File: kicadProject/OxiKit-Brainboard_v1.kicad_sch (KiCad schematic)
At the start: 60 parts, among them J1 OXY-Sensor, J10 Valve3, J11 Air Compresssor, J2 Jack-DC, J3 UART, J4 Fan1, J5 Fan2, J6 I2C, J7 Valve1, J8 Valve2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

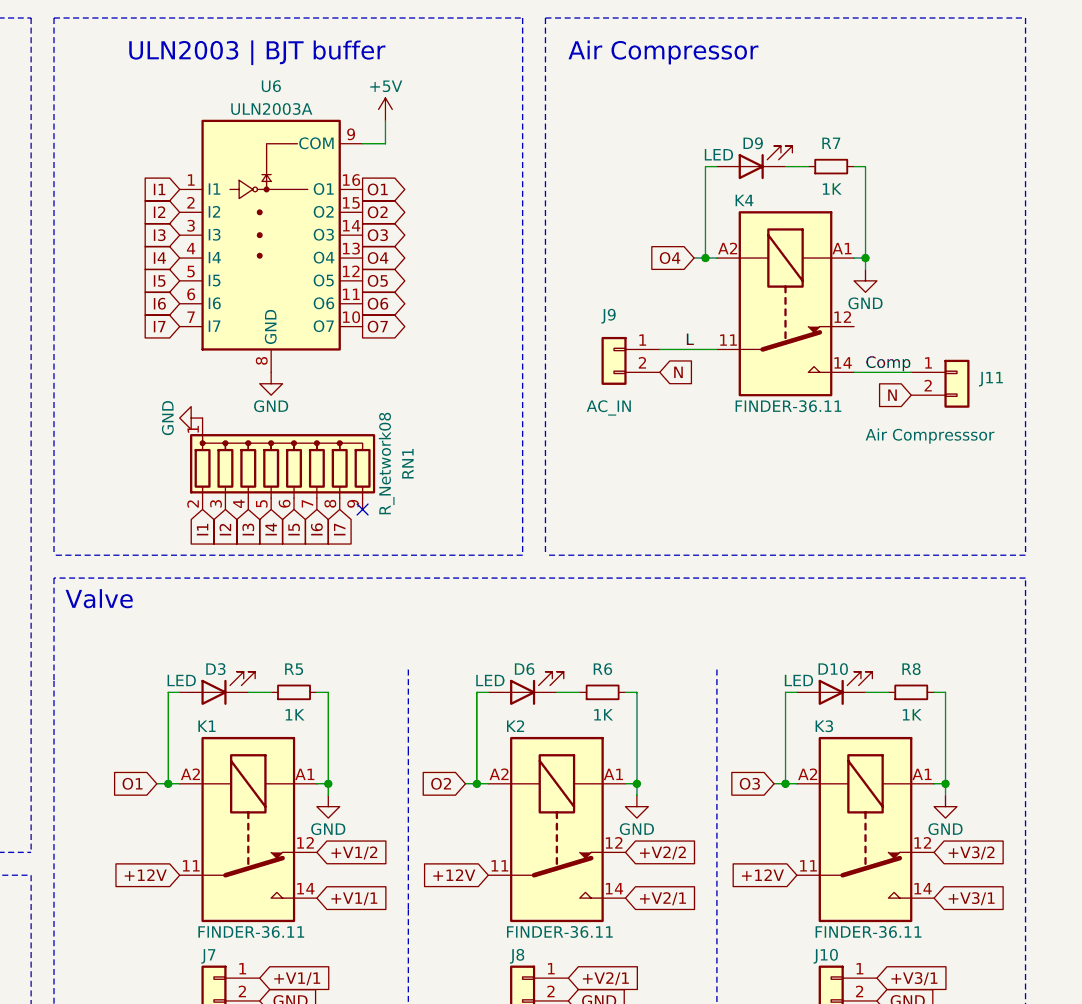
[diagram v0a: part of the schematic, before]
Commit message: #1 ULN2003 and Relay connection Fixed, Indication LED of Relay also updated
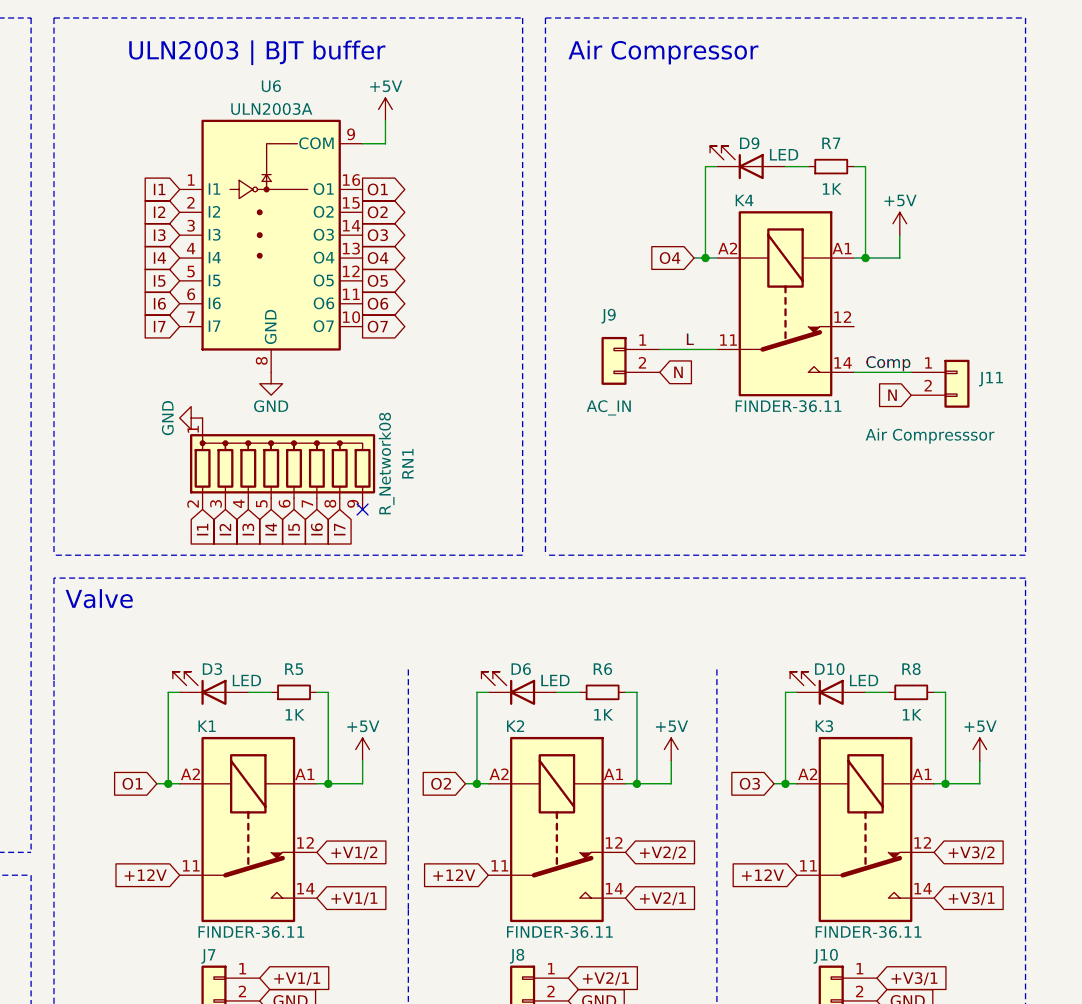
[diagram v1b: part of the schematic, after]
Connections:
- net +5V: now also K1.A1, K2.A1, K3.A1, K4.A1, R5.2, R6.2, R7.2, R8.2
- net GND: no longer K1.A1, K2.A1, K3.A1, K4.A1, R5.2, R6.2, R7.2, R8.2
- net O1: now also D3.1 (K); no longer D3.2 (A)
- net O2: now also D6.1 (K); no longer D6.2 (A)
- net O3: now also D10.1 (K); no longer D10.2 (A)
- net O4: now also D9.1 (K); no longer D9.2 (A)
- net at R7.1: now also D9.2 (A); no longer D9.1 (K)
- net at R5.1: now also D3.2 (A); no longer D3.1 (K)
- net at R8.1: now also D10.2 (A); no longer D10.1 (K)
- net at R6.1: now also D6.2 (A); no longer D6.1 (K)
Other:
- moved on the sheet: D10, D3, D6, D9

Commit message: OSHW Logo Added
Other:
- note added: "An Open Source Oxygen Concentrator Brain Board. https://github.com/shridattdudhat/Oxikit-Brainboard https://shridattdudhat.github.io"
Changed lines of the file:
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@@
     (effects (font (size 2 2)) (justify left bottom))
+  )
+  (text "An Open Source Oxygen Concentrator Brain Board.\n\nhttps://github.com/shridattdudhat/Oxikit-Brainboard\n\nhttps://shridattdudhat.github.io"
+    (at 177.8 177.8 0)
+    (effects (font (size 1.27 1.27)) (justify left bottom))
   )
   (text "ULN2003 | BJT buffer" (at 212.09 19.05 180)
@@
     (pin "1")
     (pin "2")
+  )
+  (symbol (lib_id "Graphic:Logo_Open_Hardware_Small") (at 267.97 173.99 0) (unit 1)
+    (in_bom yes) (on_board yes) (fields_autoplaced)
+    (property "Reference" "#LOGO?" (id 0) (at 267.97 167.005 0)
+      (effects (font (size 1.27 1.27)) hide)
+    )
+    (property "Value" "Logo_Open_Hardware_Small" (id 1) (at 267.97 179.705 0)
+      (effects (font (size 1.27 1.27)) hide)
+    )
+    (property "Footprint" "" (id 2) (at 267.97 173.99 0)
+      (effects (font (size 1.27 1.27)) hide)
+    )
+    (property "Datasheet" "~" (id 3) (at 267.97 173.99 0)
+      (effects (font (size 1.27 1.27)) hide)
+    )
   )
   (symbol (lib_id "Regulator_Linear:LM7805_TO220") (at 57.15 168.91 0) (unit 1)
@@
   )
   (symbol_instances
+    (path "/988d75da-a129-499a-90d8-6f1a62061a11"
+      (reference "#LOGO?") (unit 1) (value "Logo_Open_Hardware_Small") (footprint "")
+    )
     (path "/a3cbf87e-78b6-4799-99e8-c537c4416e24"
       (reference "#PWR01") (unit 1) (value "GND") (footprint "")

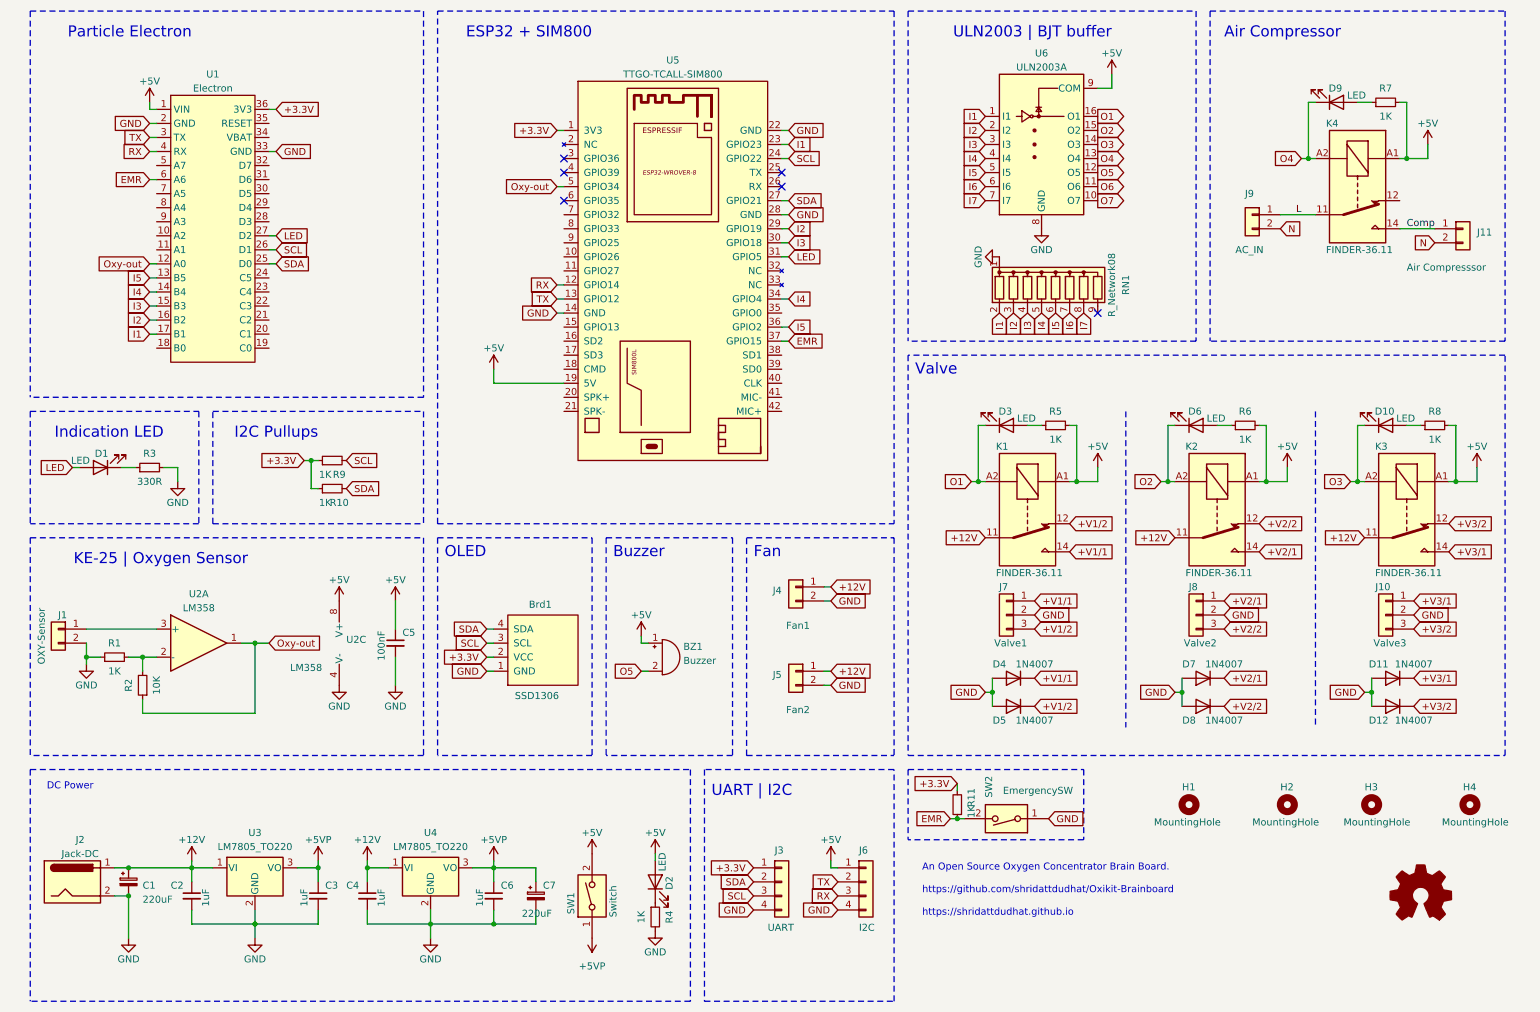
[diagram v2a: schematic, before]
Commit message: ABP Honeywell Pressure Sensor added
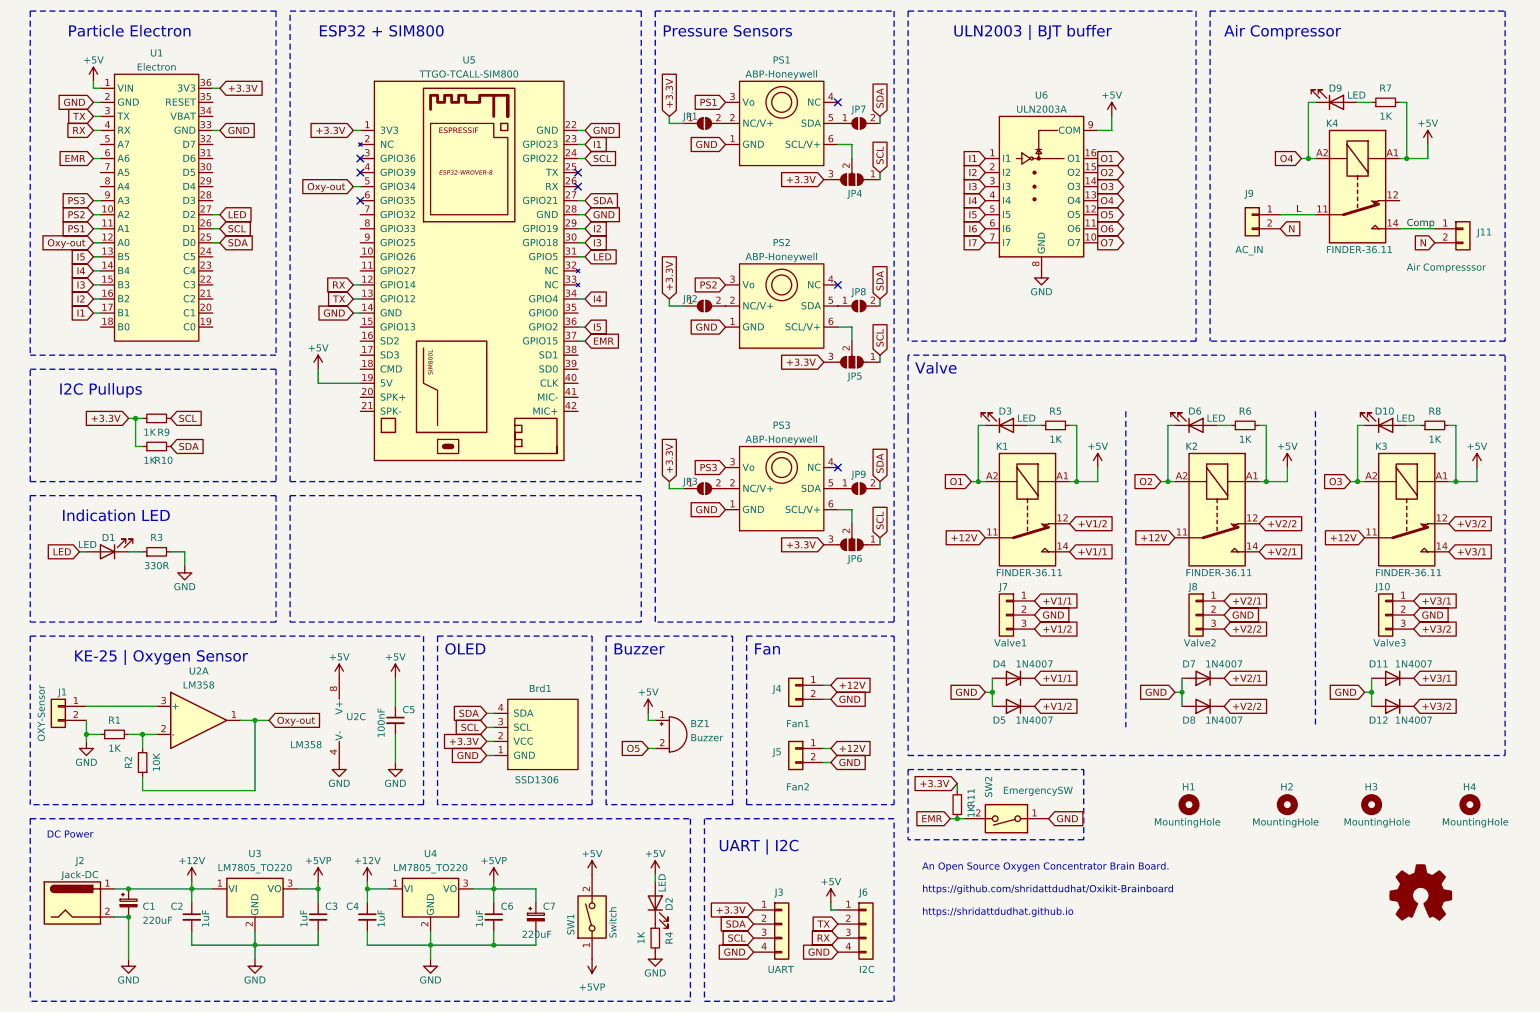
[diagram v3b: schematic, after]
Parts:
- removed RN1: R_Network08, Resistor_THT:R_Array_SIP9, symbol Device:R_Network08
- added JP1, JP2, JP3, JP7, JP8, JP9: SolderJumper_2_Open, Jumper:SolderJumper-2_P1.3mm_Open_RoundedPad1.0x1.5mm, symbol Jumper:SolderJumper_2_Open
- added JP4, JP5, JP6: SolderJumper_3_Open, Jumper:SolderJumper-3_P1.3mm_Open_RoundedPad1.0x1.5mm_NumberLabels, symbol Jumper:SolderJumper_3_Open
- added PS1, PS2, PS3: ABP-Honeywell, OxiKit-footprint-lib:ABP-Series-Pressure, symbol Oxikit-sym-lib:ABP-Honeywell
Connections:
- net +3.3V: now also JP1.1 (A), JP2.1 (A), JP3.1 (A), JP4.3 (B), JP5.3 (B), JP6.3 (B)
- net GND: now also PS1.1 (GND), PS2.1 (GND), PS3.1 (GND)
- net SCL: now also JP4.1 (A), JP5.1 (A), JP6.1 (A)
- net SDA: now also JP7.2 (B), JP8.2 (B), JP9.2 (B)
- net PS2: now reaches U1.10 (A2)
- net PS2: now also PS2.3 (Vo)
- net PS1: now reaches U1.11 (A1)
- net PS1: now also PS1.3 (Vo)
- net PS3: now reaches U1.9 (A3)
- net PS3: now also PS3.3 (Vo)
- new net: JP5.2 (C), PS2.6 (SCL/V+)
- new net: JP1.2 (B), PS1.2 (NC/V+)
- new net: JP2.2 (B), PS2.2 (NC/V+)
- new net: JP8.1 (A), PS2.5 (SDA)
- new net: JP7.1 (A), PS1.5 (SDA)
- new net: JP4.2 (C), PS1.6 (SCL/V+)
- new net: JP6.2 (C), PS3.6 (SCL/V+)
- new net: JP9.1 (A), PS3.5 (SDA)
- new net: JP3.2 (B), PS3.2 (NC/V+)
- no-connect marks 6 -> 8
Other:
- note added: "Pressure Sensors"
- moved on the sheet: BZ1, Brd1, C1, C2, C3, C4, C5, C6, C7, D1, D2, J1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

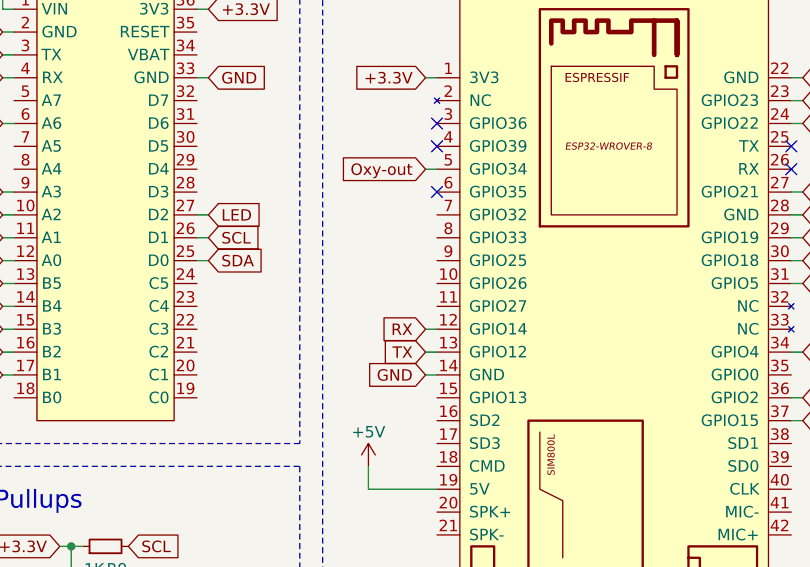
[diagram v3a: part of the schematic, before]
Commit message: Pressure Sensor connection to ESP32 #2
PS1 >> IO25
PS2 >> IO26
PS3 >> IO27
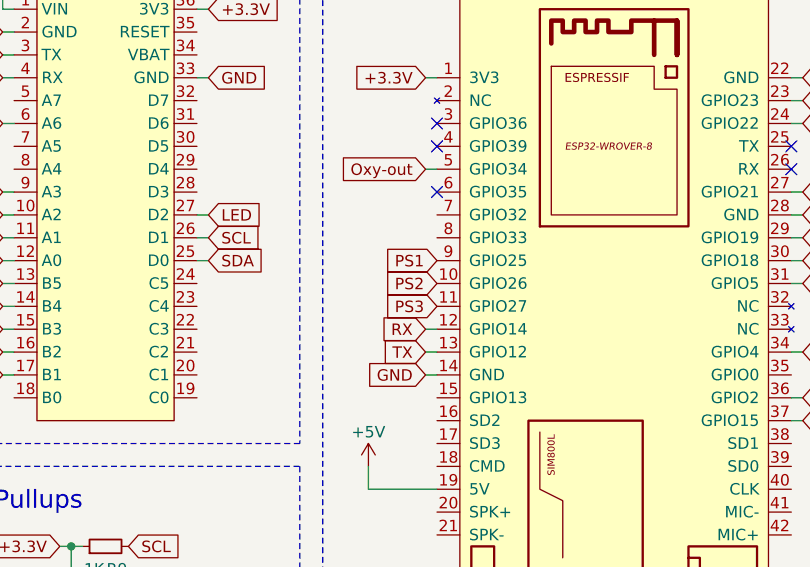
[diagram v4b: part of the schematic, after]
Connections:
- net PS1: now also U5.9 (GPIO25)
- net PS2: now also U5.10 (GPIO26)
- net PS3: now also U5.11 (GPIO27)
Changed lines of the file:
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@@
+    )
+  )
+  (global_label "PS1" (shape input) (at 76.2 55.88 180) (fields_autoplaced)
+    (effects (font (size 1.27 1.27)) (justify right))
+    (property "Intersheet References" "${INTERSHEET_REFS}" (id 0) (at 70.0979 55.8006 0)
+      (effects (font (size 1.27 1.27)) (justify right) hide)
+    )
+  )
+  (global_label "PS2" (shape input) (at 76.2 58.42 180) (fields_autoplaced)
+    (effects (font (size 1.27 1.27)) (justify right))
+    (property "Intersheet References" "${INTERSHEET_REFS}" (id 0) (at 70.0979 58.3406 0)
+      (effects (font (size 1.27 1.27)) (justify right) hide)
+    )
+  )
+  (global_label "PS3" (shape input) (at 76.2 60.96 180) (fields_autoplaced)
+    (effects (font (size 1.27 1.27)) (justify right))
+    (property "Intersheet References" "${INTERSHEET_REFS}" (id 0) (at 70.0979 60.8806 0)
+      (effects (font (size 1.27 1.27)) (justify right) hide)
     )
   )
